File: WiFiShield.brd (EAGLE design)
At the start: 68.6 x 53.3 mm, 35 parts, among them IC1 MC74VHCT50A, IC2 74AHC1G125, IC4 SPX3819M5-L-3-3, IC5 CC3000MOD, J10 Test, J2 Mode, J8 ARDUINO-SHIELD_R3, J9 U.FL-R-SMT-1(10)

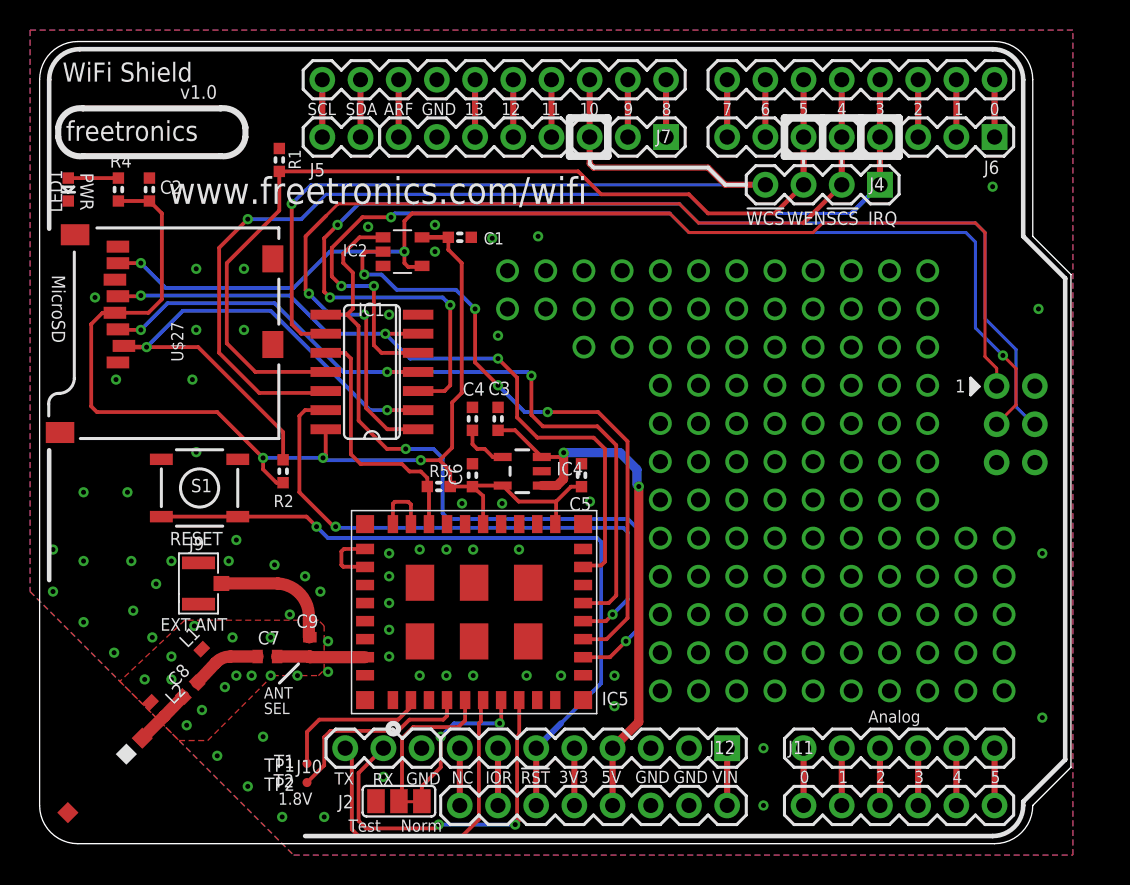
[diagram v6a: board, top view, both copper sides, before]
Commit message: Swap SPX3819 LDO for AP2112K-3.3
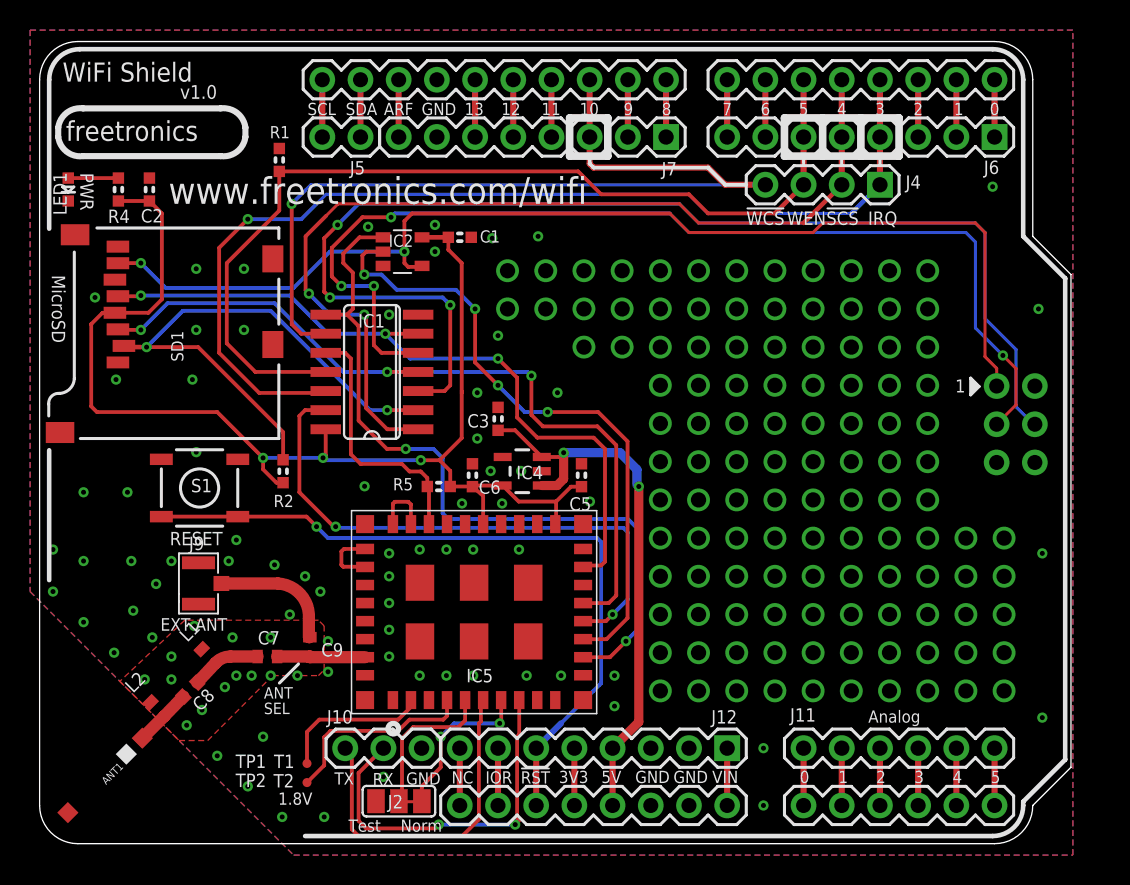
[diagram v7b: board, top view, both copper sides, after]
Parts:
- removed C4: 10nF, freetronics-master-v1:0603
- IC4: value SPX3819M5-L-3-3 -> AP2112K-3.3; device SparkFun:SOT23-5 -> freetronics-angus:SOT23-5
- renumbered U$27 to SD1
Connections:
- removed net N$43: C4.2, IC4.4
- net GND: no longer C4.1
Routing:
- net N$43: track 3.29 -> 0.00 mm
